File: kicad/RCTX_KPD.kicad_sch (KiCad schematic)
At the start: 32 parts

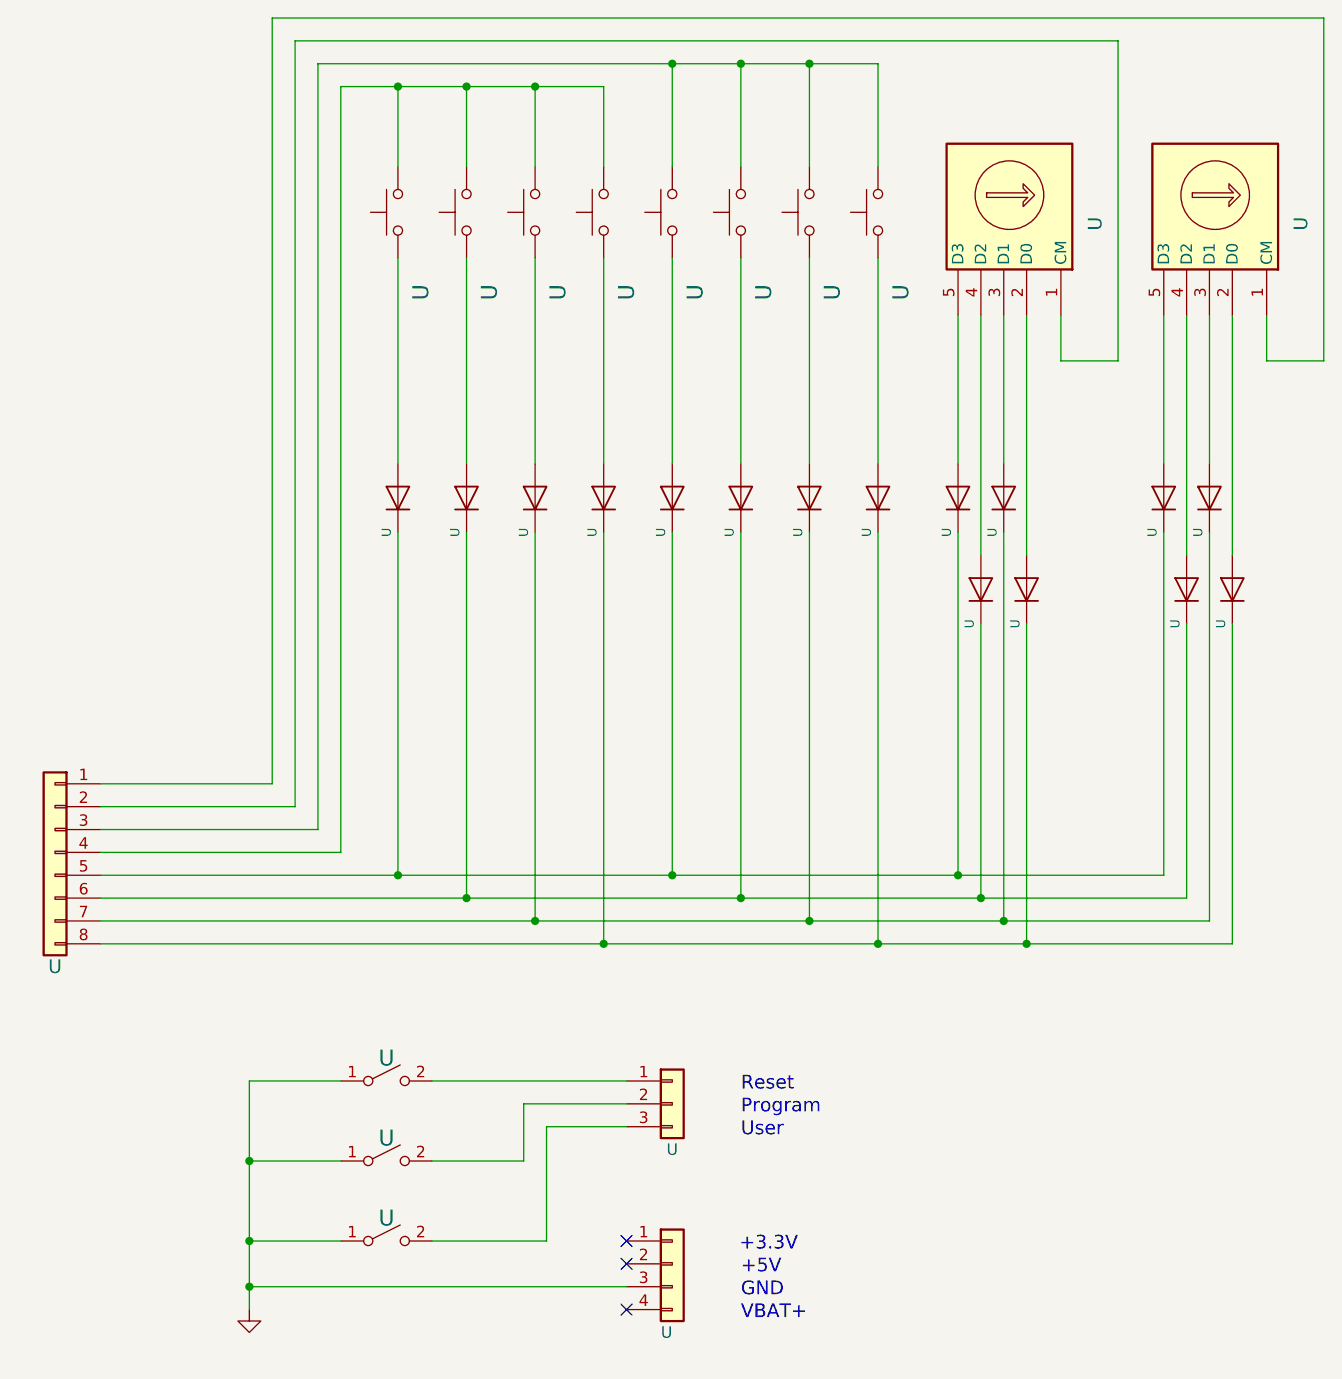
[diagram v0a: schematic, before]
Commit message: Adding PIB USB BRIDGE UML state diagrams - WIP
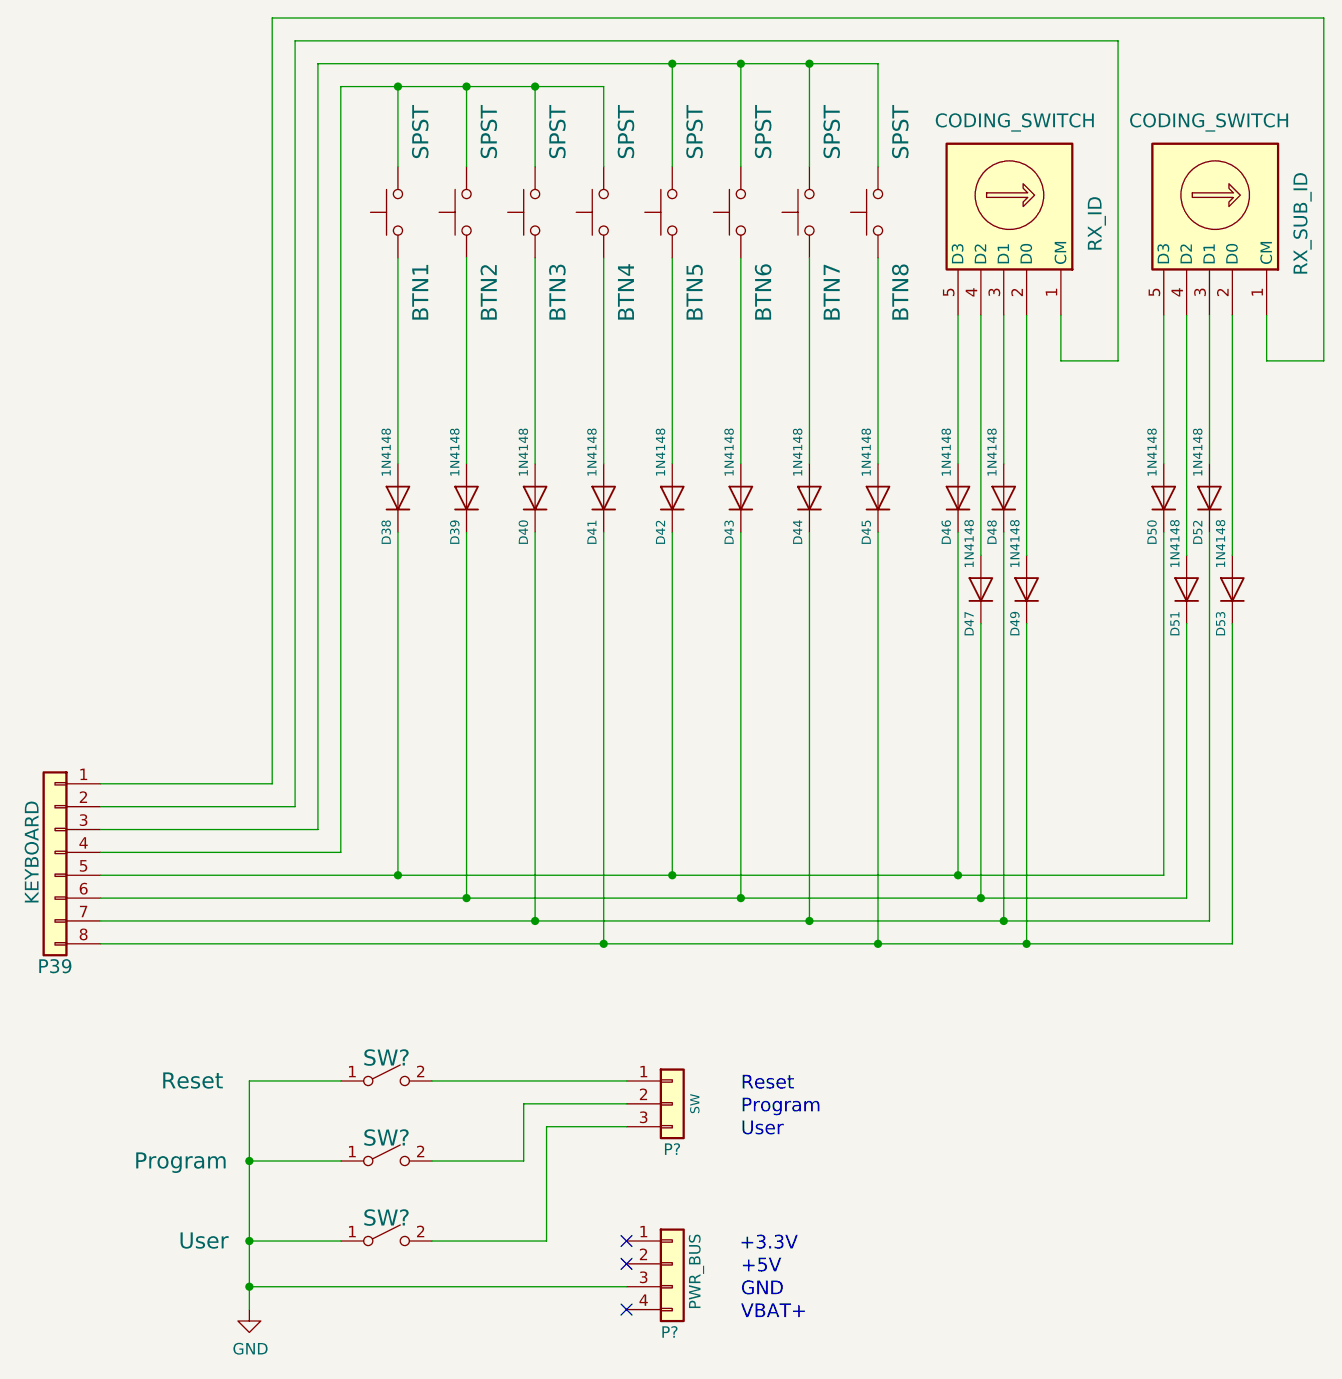
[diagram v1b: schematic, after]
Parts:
- BTN1, BTN2, BTN3, BTN4, BTN5, BTN6, BTN7, BTN8: renamed from U; value (none) -> SPST; footprint (none) -> Buttons_Switches_THT:SW_PUSH_6mm_h5mm
- D38, D39, D40, D41, D42, D43, D44, D45, D46, D47, D48, D49, D50, D51, D52, D53: renamed from U; value (none) -> 1N4148; footprint (none) -> Diodes_THT:D_5W_P5.08mm_Vertical_KathodeUp
- P39: renamed from U; value (none) -> KEYBOARD; footprint (none) -> Connectors_Samtec:SL-108-X-XX_1x08
- P?: renamed from U; value (none) -> SW; footprint (none) -> Connectors_Samtec:SL-103-X-XX_1x03
- P?: renamed from U; value (none) -> PWR_BUS; footprint (none) -> Connectors_Samtec:SL-104-X-XX_1x04
- RX_ID, RX_SUB_ID: renamed from U; value (none) -> CODING_SWITCH; footprint (none) -> Buttons_Switches_THT:Nidec_Copal_SH-7010C
- SW?: renamed from U; value (none) -> Reset; footprint (none) -> Buttons_Switches_THT:SW_PUSH_6mm_h5mm
- SW?: renamed from U; value (none) -> Program; footprint (none) -> Buttons_Switches_THT:SW_PUSH_6mm_h5mm
- SW?: renamed from U; value (none) -> User; footprint (none) -> Buttons_Switches_THT:SW_PUSH_6mm_h5mm
